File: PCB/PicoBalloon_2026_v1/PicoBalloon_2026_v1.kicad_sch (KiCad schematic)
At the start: 50 parts, among them J1 Conn_01x07_Pin, J10 Conn_01x02_Pin, J11 Conn_01x01_Pin, J2 Conn_01x04_Pin, J3 Conn_01x02_Pin, J4 Conn_01x02_Pin, J5 Conn_01x02_Pin, J6 Conn_01x02_Pin, J7 Conn_01x02_Pin, J8 Conn_01x02_Pin, J9 Conn_01x04_Pin, Q1 FDV304P, Q2 FDV304P, U1 ATmega328P-A, U2 RFM95W-868S2, U3 GP-02, U5 TS5205CX525, Y1 8MHz

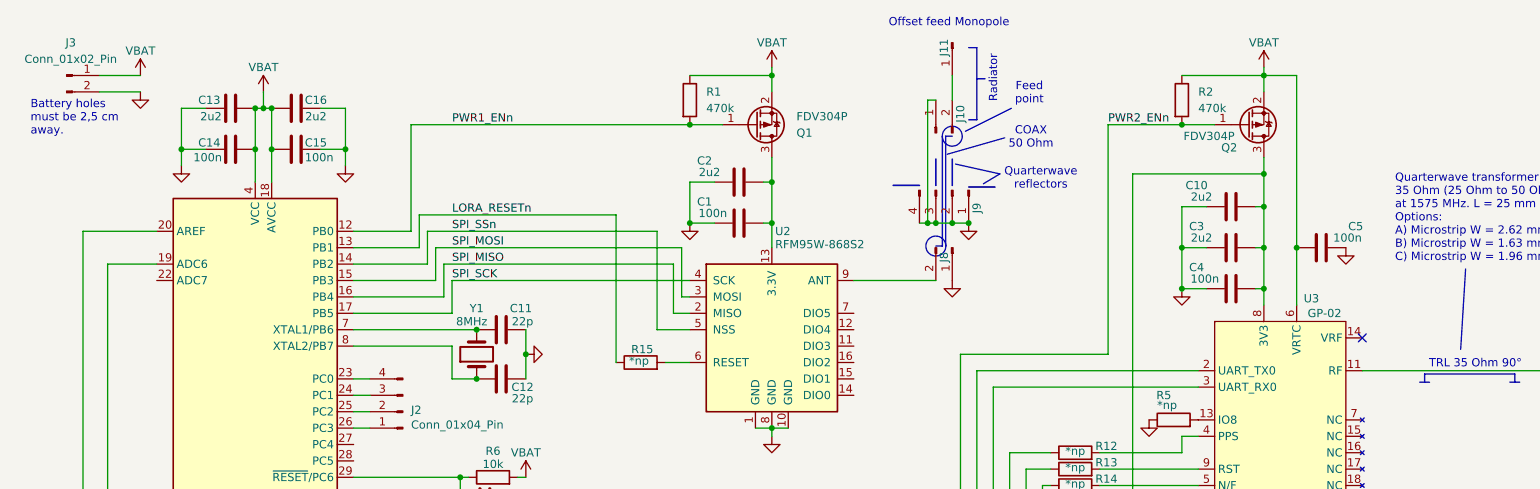
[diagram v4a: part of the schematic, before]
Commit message: [PCB] PCB design begin.
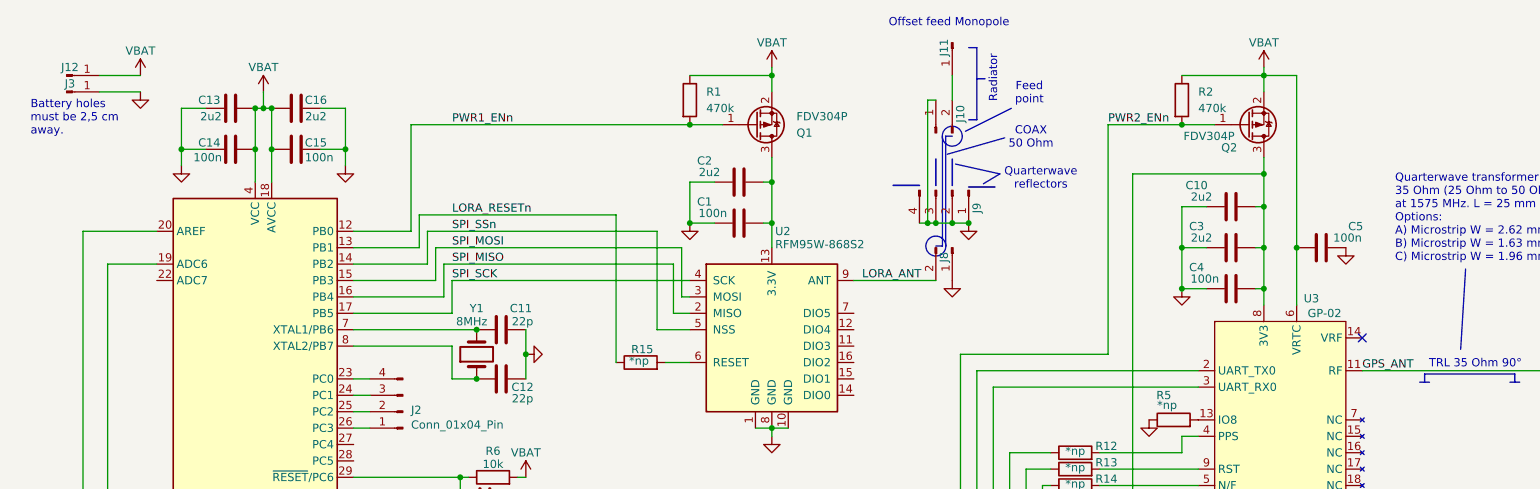
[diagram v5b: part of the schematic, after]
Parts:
- removed J3: Conn_01x02_Pin, Connector_PinHeader_2.54mm:PinHeader_1x02_P2.54mm_Vertical, symbol Connector:Conn_01x02_Pin
- added J12, J3: Conn_01x01_Pin, Connector_PinHeader_2.54mm:PinHeader_1x01_P2.54mm_Vertical, symbol Connector:Conn_01x01_Pin
- U3: footprint (none) -> GP-02_GPS_module:GP-02
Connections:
- net GND: now also J3.1 (Pin_1)
- net VBAT: now also J12.1 (Pin_1)
- net LORA_ANT: now reaches J8.2 (Pin_2), U2.9 (ANT)
- net GPS_ANT: now reaches J4.1 (Pin_1), J4.2 (Pin_2), U3.11 (RF)
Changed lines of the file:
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@@
 		)
 	)
+	(label "GPS_ANT"
+		(at 224.79 68.58 0)
+		(effects
+			(font
+				(size 1.27 1.27)
+			)
+			(justify left bottom)
+		)
+	)
+	(label "LORA_ANT"
+		(at 147.32 54.61 0)
+		(effects
+			(font
+				(size 1.27 1.27)
+			)
+			(justify left bottom)
+		)
+	)
 	(label "GPS_TX_SILENTn"
 		(at 102.87 121.92 90)
@@
 	)
 	(symbol
+		(lib_id "Connector:Conn_01x01_Pin")
+		(at 24.13 22.86 0)
+		(unit 1)
+		(exclude_from_sim no)
+		(in_bom yes)
+		(on_board yes)
+		(dnp no)
+		(property "Reference" "J12"
+			(at 24.638 21.59 0)
+			(effects
+				(font
+					(size 1.27 1.27)
+				)
+			)
+		)
+		(property "Value" "Conn_01x01_Pin"
+			(at 24.765 20.32 0)
+			(effects
+				(font
+					(size 1.27 1.27)
+				)
+				(hide yes)
+			)
+		)
+		(property "Footprint" "Connector_PinHeader_2.54mm:PinHeader_1x01_P2.54mm_Vertical"
+			(at 24.13 22.86 0)
+			(effects
+				(font
+					(size 1.27 1.27)
+				)
+				(hide yes)
+			)
+		)
+		(property "Datasheet" "~"
+			(at 24.13 22.86 0)
+			(effects
+				(font
+					(size 1.27 1.27)
+				)
+				(hide yes)
+			)
+		)
+		(property "Description" "Generic connector, single row, 01x01, script generated"
+			(at 24.13 22.86 0)
+			(effects
+				(font
+					(size 1.27 1.27)
+				)
+				(hide yes)
+			)
+		)
+		(pin "1"
+		)
+		(instances
+			(project ""
+				(path "/5830a2be-f2a8-4c09-97d5-19df3de68a31"
+					(reference "J12")
+					(unit 1)
+				)
+			)
+		)
+	)
+	(symbol
 		(lib_id "power:VCC")
 		(at 238.76 93.98 0)
@@
 	)
 	(symbol
+		(lib_id "Connector:Conn_01x01_Pin")
+		(at 24.13 25.4 0)
+		(unit 1)
+		(exclude_from_sim no)
+		(in_bom yes)
+		(on_board yes)
+		(dnp no)
+		(property "Reference" "J3"
+			(at 24.638 24.13 0)
+			(effects
+				(font
+					(size 1.27 1.27)
+				)
+			)
+		)
+		(property "Value" "Conn_01x01_Pin"
+			(at 24.765 22.86 0)
+			(effects
+				(font
+					(size 1.27 1.27)
+				)
+				(hide yes)
+			)
+		)
+		(property "Footprint" "Connector_PinHeader_2.54mm:PinHeader_1x01_P2.54mm_Vertical"
+			(at 24.13 25.4 0)
+			(effects
+				(font
+					(size 1.27 1.27)
+				)
+				(hide yes)
+			)
+		)
+		(property "Datasheet" "~"
+			(at 24.13 25.4 0)
+			(effects
+				(font
+					(size 1.27 1.27)
+				)
+				(hide yes)
+			)
+		)
+		(property "Description" "Generic connector, single row, 01x01, script generated"
+			(at 24.13 25.4 0)
+			(effects
+				(font
+					(size 1.27 1.27)
+				)
+				(hide yes)
+			)
+		)
+		(pin "1"
+		)
+		(instances
+			(project "PicoBalloon_2026_v1"
+				(path "/5830a2be-f2a8-4c09-97d5-19df3de68a31"
+					(reference "J3")
+					(unit 1)
+				)
+			)
+		)
+	)
+	(symbol
 		(lib_id "power:GND")
 		(at 205.74 124.46 0)
@@
 	)
 	(symbol
-		(lib_id "Connector:Conn_01x02_Pin")
-		(at 24.13 22.86 0)
-		(unit 1)
-		(exclude_from_sim no)
-		(in_bom yes)
-		(on_board yes)
-		(dnp no)
-		(fields_autoplaced yes)
-		(property "Reference" "J3"
-			(at 24.765 17.78 0)
-			(effects
-				(font
-					(size 1.27 1.27)
-				)
-			)
-		)
-		(property "Value" "Conn_01x02_Pin"
-			(at 24.765 20.32 0)
-			(effects
-				(font
-					(size 1.27 1.27)
-				)
-			)
-		)
-		(property "Footprint" "Connector_PinHeader_2.54mm:PinHeader_1x02_P2.54mm_Vertical"
-			(at 24.13 22.86 0)
-			(effects
-				(font
-					(size 1.27 1.27)
-				)
-				(hide yes)
-			)
-		)
-		(property "Datasheet" "~"
-			(at 24.13 22.86 0)
-			(effects
-				(font
-					(size 1.27 1.27)
-				)
-				(hide yes)
-			)
-		)
-		(property "Description" "Generic connector, single row, 01x02, script generated"
-			(at 24.13 22.86 0)
-			(effects
-				(font
-					(size 1.27 1.27)
-				)
-				(hide yes)
-			)
-		)
-		(pin "1"
-		)
-		(pin "2"
-		)
-		(instances
-			(project ""
-				(path "/5830a2be-f2a8-4c09-97d5-19df3de68a31"
-					(reference "J3")
-					(unit 1)
-				)
-			)
-		)
-	)
-	(symbol
 		(lib_id "power:GND")
 		(at 219.71 129.54 0)
@@
 			)
 		)
-		(property "Footprint" ""
+		(property "Footprint" "GP-02_GPS_module:GP-02"
 			(at 212.09 74.93 0)
 			(effects

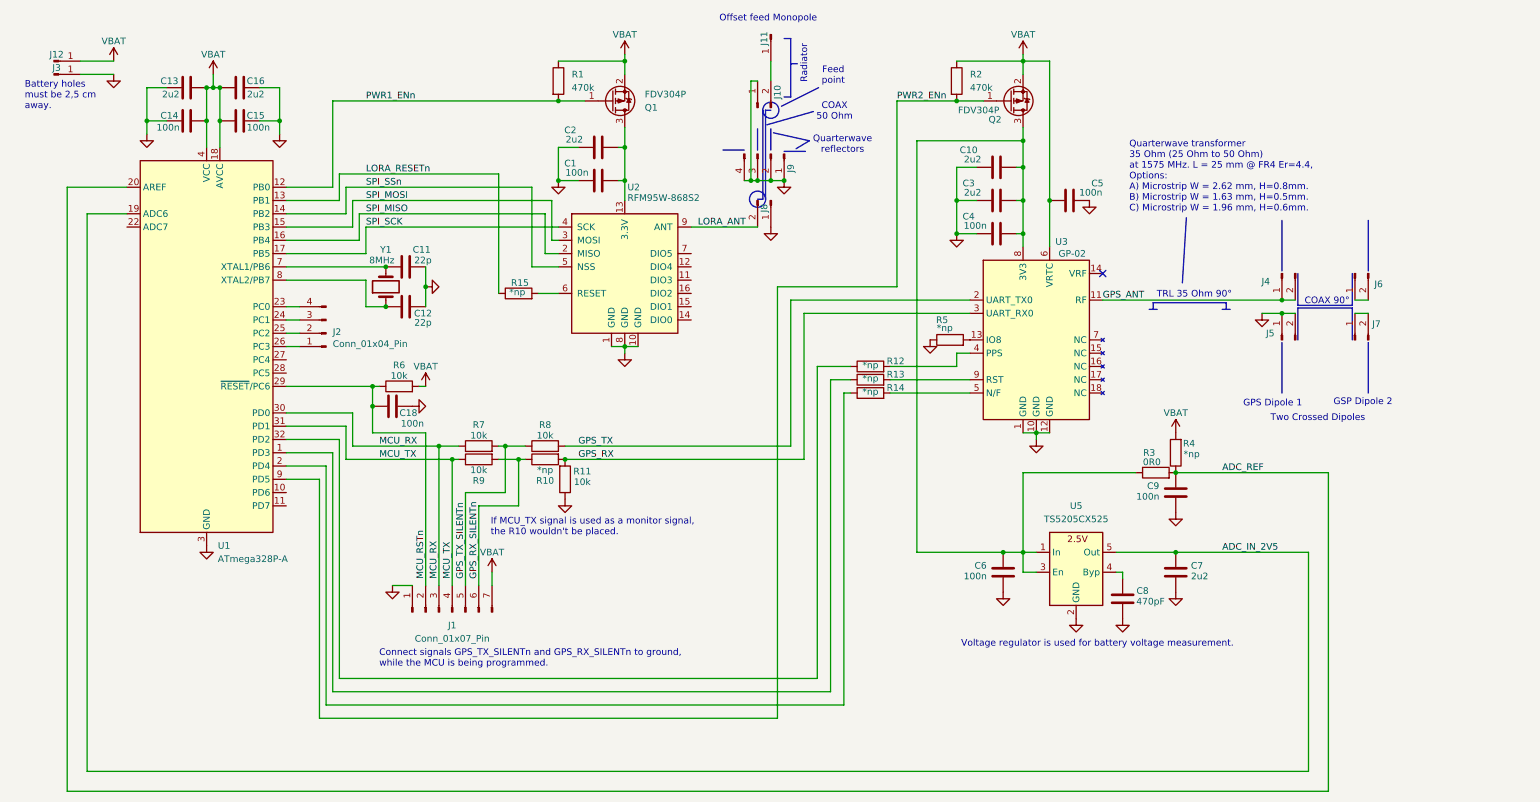
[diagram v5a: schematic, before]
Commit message: [PCB] PCB finished! (I hope). Not so critical signals removed. Voltage regulator removed because it is not needed.
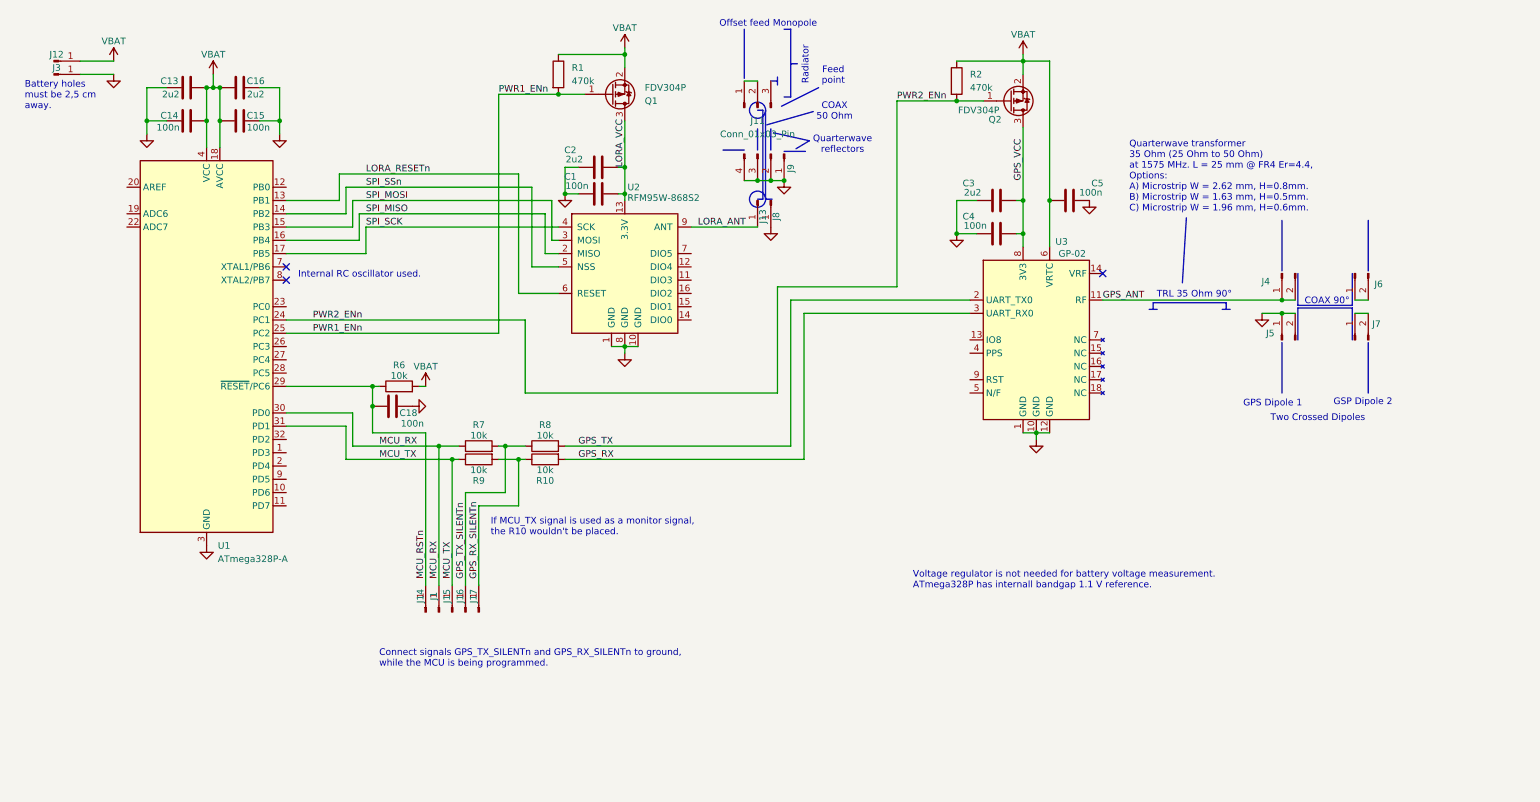
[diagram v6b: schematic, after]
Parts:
- removed C10, C7: 2u2, Capacitor_SMD:C_0805_2012Metric_Pad1.18x1.45mm_HandSolder, symbol Device:C
- removed C11, C12: 22p, Capacitor_SMD:C_0805_2012Metric_Pad1.18x1.45mm_HandSolder, symbol Device:C
- removed C6, C9: 100n, Capacitor_SMD:C_0805_2012Metric_Pad1.18x1.45mm_HandSolder, symbol Device:C
- removed C8: 470pF, Capacitor_SMD:C_0805_2012Metric_Pad1.18x1.45mm_HandSolder, symbol Device:C
- removed J1: Conn_01x07_Pin, Connector_PinHeader_2.54mm:PinHeader_1x07_P2.54mm_Vertical, symbol Connector:Conn_01x07_Pin
- removed J10, J8: Conn_01x02_Pin, Connector_PinHeader_1.00mm:PinHeader_1x02_P1.00mm_Vertical, symbol Connector:Conn_01x02_Pin
- removed J11: Conn_01x01_Pin, Connector_Wire:SolderWirePad_1x01_SMD_2x4mm, symbol Connector:Conn_01x01_Pin
- removed J2: Conn_01x04_Pin, Connector_PinHeader_2.54mm:PinHeader_1x04_P2.54mm_Vertical, symbol Connector:Conn_01x04_Pin
- removed R11: 10k, Resistor_SMD:R_0805_2012Metric_Pad1.20x1.40mm_HandSolder, symbol Device:R
- removed R12, R13, R14, R15, R4, R5: *np, Resistor_SMD:R_0805_2012Metric_Pad1.20x1.40mm_HandSolder, symbol Device:R
- removed R3: 0R0, Resistor_SMD:R_0805_2012Metric_Pad1.20x1.40mm_HandSolder, symbol Device:R
- removed U5: TS5205CX525, Package_TO_SOT_SMD:SOT-23-5, symbol Jozka_Library:TS5205
- removed Y1: 8MHz, Crystal:Crystal_SMD_HC49-SD, symbol Device:Crystal
- added J1, J14, J15, J16, J17: Conn_01x01_Pin, Connector_Wire:SolderWirePad_1x01_SMD_1x2mm, symbol Connector:Conn_01x01_Pin
- added J11: Conn_01x03_Pin, Connector_PinHeader_1.27mm:PinHeader_1x03_P1.27mm_Vertical, symbol Connector:Conn_01x03_Pin
- added J13, J8: Conn_01x01_Pin, Connector_PinHeader_1.27mm:PinHeader_1x01_P1.27mm_Vertical, symbol Connector:Conn_01x01_Pin
- J4, J5, J6, J7: footprint Connector_PinHeader_2.54mm:PinHeader_1x02_P2.54mm_Vertical -> Connector_PinHeader_1.27mm:PinHeader_1x02_P1.27mm_Vertical
- J9: footprint Connector_PinHeader_2.54mm:PinHeader_1x04_P2.54mm_Vertical -> Connector_PinHeader_1.27mm:PinHeader_1x04_P1.27mm_Vertical
- R10: value *np -> 10k
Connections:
- net GND: now also J8.1 (Pin_1)
- net GPS_RX_SILENTn: now also J17.1 (Pin_1)
- net GPS_TX_SILENTn: now also J16.1 (Pin_1)
- net LORA_ANT: now also J13.1 (Pin_1)
- net LORA_RESETn: now also U2.6 (RESET)
- net MCU_RSTn: now also J14.1 (Pin_1)
- net MCU_RX: now also J1.1 (Pin_1)
- net MCU_TX: now also J15.1 (Pin_1)
- net PWR1_ENn: now also U1.25 (PC2); no longer U1.12 (PB0)
- net PWR2_ENn: now also U1.24 (PC1); no longer U1.9 (PD5)
- net GPS_VCC: now reaches C3.2, C4.2, Q2.3 (D), U3.8 (3V3)
- net LORA_VCC: now reaches C1.2, C2.2, Q1.3 (D), U2.13 (3.3V)
- net ADC_IN_2V5: no longer names the net of U1.19 (ADC6)
- net ADC_REF: no longer names the net of U1.20 (AREF)
- new net: J11.1 (Pin_1), J11.2 (Pin_2)
- no-connect marks 1 -> 3
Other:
- note added: "Internal RC oscillator used."
- note added: "Voltage regulator is not needed for battery voltage measurement. ATmega328P has internall bandgap 1.1 V reference."
- note removed: "Voltage regulator is used for battery voltage measurement."
- moved on the sheet: C1, C2, Q1, R1
